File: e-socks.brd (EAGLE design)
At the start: 65.1 x 30 mm, 91 parts, among them IC1 CC2540, IC2 741G240DCK, IC3 TPS6300X, P2 TMAV433BAA, Q1 FA-20H(32MHz), Q2 ABS06, U2 MAX21000, X4 1296-T10

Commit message: erstes commit für diesen branch
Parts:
- removed C1: 100nF, rcl:C0402
- removed IC3: TPS6300X, m_vreg:S-PVSON-N10
- removed L1: CR32, inductors:CR32
- added LED3, LED4: Blue/2.9V@10mA, led:CHIP-LED0603
- added R8: 47RR, rcl:R0402
- C5, C6: value 10µF -> 22µF; device rcl:C0603 -> rcl:C0805
- R6: value 100R -> 47RR
- moved R6 24.7 mm to (19.6, 27.4), turned to 90 degrees
- moved L3 11.0 mm to (3.62, 16.6), turned to 270 degrees
- moved C9 10.5 mm to (6.29, 8.83)
- moved IC7 10.4 mm to (6.99, 10.7)
- moved R5 8.84 mm to (4.32, 8.64), turned to 90 degrees
- moved R3 6.46 mm to (3.68, 10.5), turned to 180 degrees
- moved C2 5.05 mm to (8.64, 14.4)
- moved C6 1.36 mm to (12.9, 10.8), turned to 270 degrees
- moved C5 0.77 mm to (11.0, 10.7), turned to 270 degrees
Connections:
- removed net N$10: C1.2, IC3.7, IC3.8, R6.2
- removed net VOUT: IC7.7
- net +5V: now also IC7.7; no longer IC3.1
- net 5V_ENABLE: now also IC7.2; no longer IC3.6
- net GND: now also LED3.C, LED4.C; no longer C1.1, IC3.3, IC3.9, IC3.PAD
- net HEATER1_PWR: now also R8.1
- net HEATER2_PWR: now also R6.1
- net N$1: now also LED3.A, R6.2; no longer IC3.4, L1.1
- net N$3: now also LED4.A, R8.2; no longer IC3.2, L1.2
- net N$4: now also IC7.3; no longer IC3.10
- net VBAT: no longer IC3.5, R6.1
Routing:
- net VBAT: track 56.3 -> 49.1 mm
- net +5V: track 1.65 -> 8.33 mm
- net N$4: track 7.31 -> 3.15 mm, vias 2 -> 0
- net N$1: track 3.42 -> 0.00 mm
- net N$3: track 3.42 -> 0.00 mm
- net N$10: track 3.20 -> 0.00 mm
- net N$6: track 0.00 -> 1.28 mm
- net 5V_ENABLE: track 31.9 -> 30.9 mm
- added copper zone on layer 1, net N$5

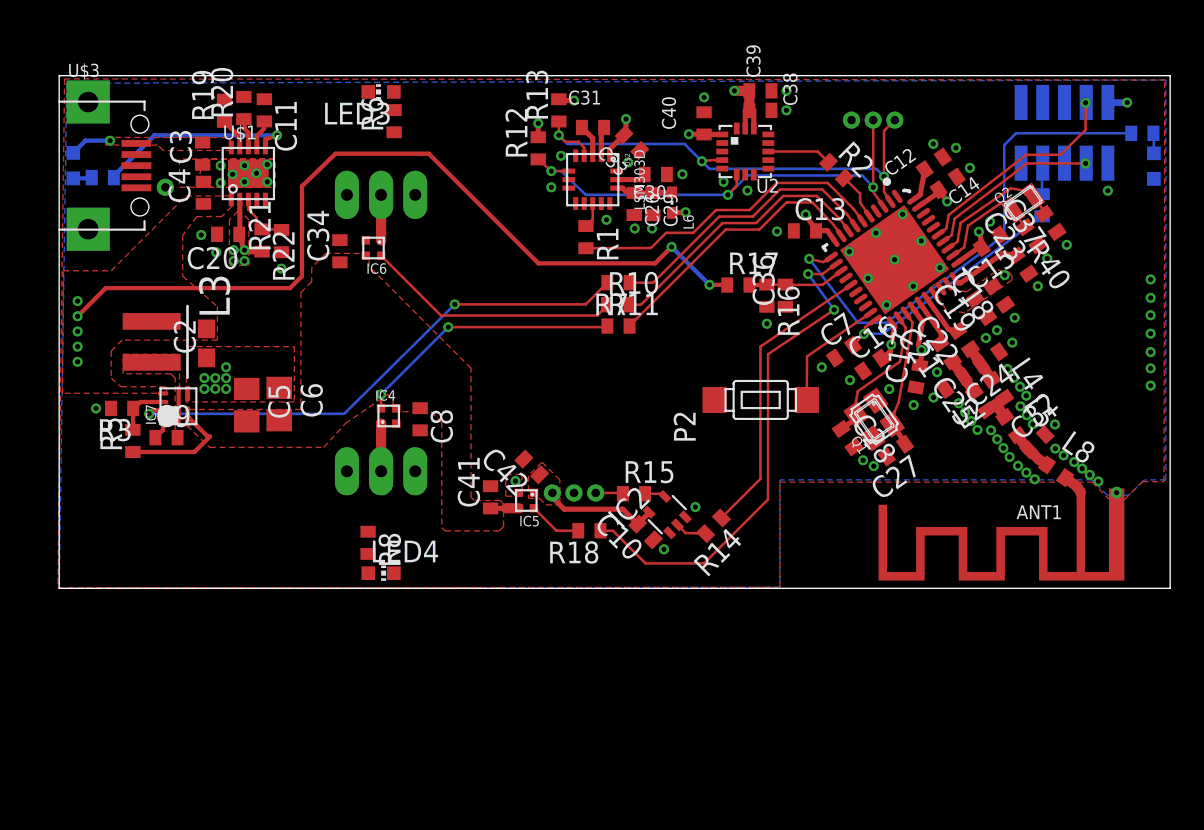
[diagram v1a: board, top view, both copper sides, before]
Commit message: taster getauscht, 2.5mm klinke hinzugefügt, noch nicht geroutet
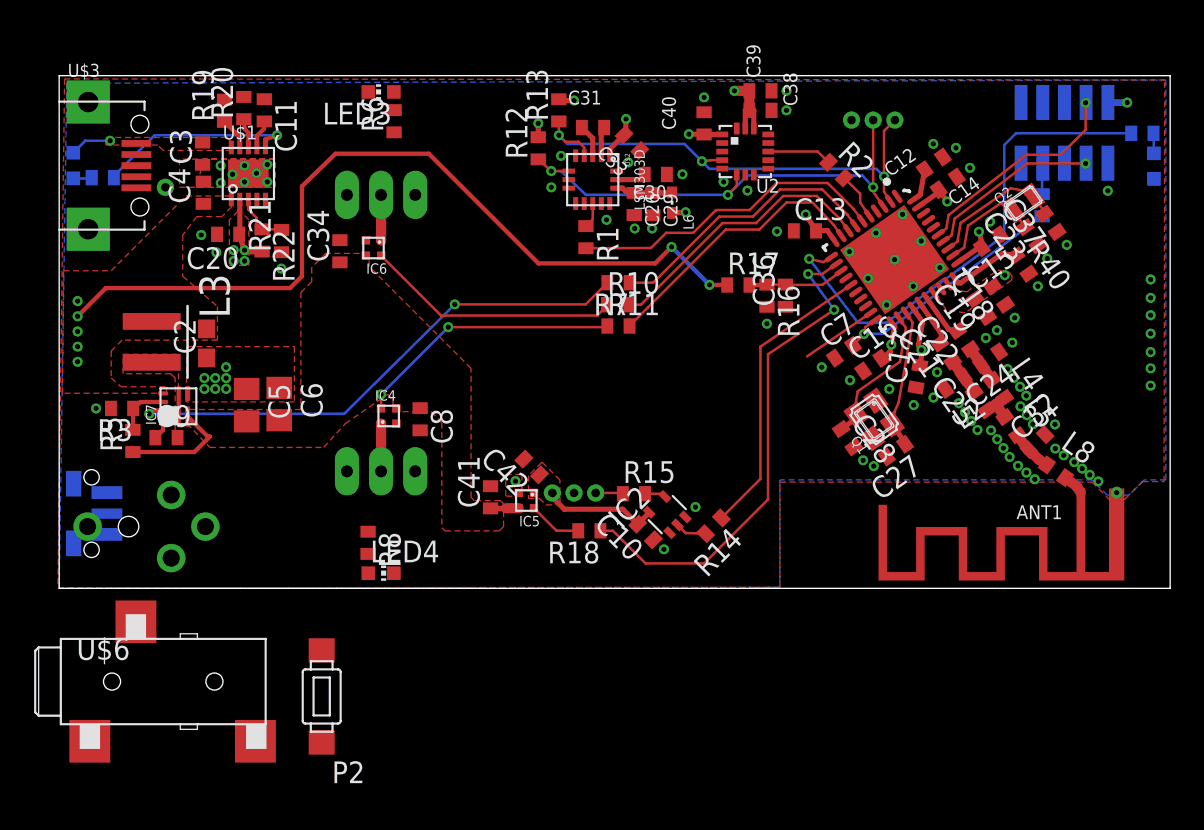
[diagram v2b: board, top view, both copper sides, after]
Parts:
- added S1: TL3340AF160QG, SamacSys_Parts:TL3340
- added U$6: SJ-2523-SMT, con-cuistack:SJ-2523-SMT
- added U$7: SJ-2503A, con-cuistack:SJ-2503
- moved P2 31.0 mm to (15.4, -6.33), turned to 180 degrees
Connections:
- net GND: now also S1.1, S1.3, U$6.1, U$7.1
- net LS2812_PWR: now also U$6.3, U$7.4
- net SW1: now also S1.2
- net WS2812B_OUT: now also U$6.2, U$7.2
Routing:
- net SW1: track 7.06 -> 4.50 mm
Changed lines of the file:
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@@
 <layer number="14" name="Route14" color="1" fill="6" visible="no" active="no"/>
 <layer number="15" name="Route15" color="4" fill="6" visible="no" active="yes"/>
-<layer number="16" name="Bottom" color="1" fill="1" visible="yes" active="yes"/>
+<layer number="16" name="Bottom" color="1" fill="1" visible="no" active="yes"/>
 <layer number="17" name="Pads" color="2" fill="1" visible="yes" active="yes"/>
 <layer number="18" name="Vias" color="2" fill="1" visible="yes" active="yes"/>
@@
 <layer number="22" name="bPlace" color="7" fill="1" visible="yes" active="yes"/>
 <layer number="23" name="tOrigins" color="15" fill="1" visible="yes" active="yes"/>
-<layer number="24" name="bOrigins" color="15" fill="1" visible="no" active="yes"/>
+<layer number="24" name="bOrigins" color="15" fill="1" visible="yes" active="yes"/>
 <layer number="25" name="tNames" color="7" fill="1" visible="no" active="yes"/>
 <layer number="26" name="bNames" color="7" fill="1" visible="no" active="yes"/>
@@
 <layer number="39" name="tKeepout" color="4" fill="11" visible="no" active="yes"/>
 <layer number="40" name="bKeepout" color="1" fill="11" visible="no" active="yes"/>
-<layer number="41" name="tRestrict" color="4" fill="10" visible="no" active="yes"/>
+<layer number="41" name="tRestrict" color="4" fill="10" visible="yes" active="yes"/>
 <layer number="42" name="bRestrict" color="1" fill="10" visible="no" active="yes"/>
 <layer number="43" name="vRestrict" color="2" fill="10" visible="no" active="yes"/>
@@
 <board>
 <plain>
+<wire x1="51.6255" y1="16.637" x2="52.705" y2="15.8115" width="0" layer="41"/>
 <wire x1="52.705" y1="15.8115" x2="56.007" y2="11.1125" width="0" layer="41"/>
 <wire x1="55.499" y1="10.7315" x2="56.896" y2="8.6995" width="0" layer="41"/>
@@
 <element name="Q1" library="crystal-epson" package="FA-20H" value="FA-20H(32MHz)" x="47.74906875" y="9.89306875" rot="R125"/>
 <element name="L8" library="rcl-2" package="L0402" value="3N0" x="58.402075" y="6.85911875" rot="R325"/>
-<element name="P2" library="switch-misc" package="TMAV433BAA" value="TMAV433BAA" x="41.100346875" y="11.036846875" rot="R90"/>
+<element name="P2" library="switch-misc" package="TMAV433BAA" value="TMAV433BAA" x="15.379153125" y="-6.334153125" rot="R180"/>
 <element name="C4" library="resistor" package="C0402" value="2,2µF" x="8.4455" y="23.1775" rot="R90"/>
 <element name="C3" library="rcl" package="C0402" value="4,7µF" x="8.404" y="25.465" rot="R90"/>
@@
 <element name="R8" library="rcl" package="R0402" value="47RR" x="18.0975" y="2.667" rot="R270"/>
 <element name="LED4" library="led" package="CHIP-LED0603" value="Blue/2.9V@10mA" x="18.8595" y="0.889" rot="R270"/>
+<element name="S1" library="SamacSys_Parts" package="TL3340" value="TL3340AF160QG" x="0.6985" y="4.3815" rot="MR90">
+<attribute name="DESCRIPTION" value="E-SWITCH - TL3340AF160QG. - SWITCH, TACTILE SPST 50mA, SMD GULL WING" x="0.6985" y="4.3815" size="1.778" layer="28" rot="MR90" display="off"/>
+<attribute name="HEIGHT" value="mm" x="0.6985" y="4.3815" size="1.778" layer="28" rot="MR90" display="off"/>
+<attribute name="MOUSER_PART_NUMBER" value="612-TL3340AF160QG" x="0.6985" y="4.3815" size="1.778" layer="28" rot="MR90" display="off"/>
+<attribute name="MANUFACTURER_NAME" value="E-Switch" x="0.6985" y="4.3815" size="1.778" layer="28" rot="MR90" display="off"/>
+<attribute name="MANUFACTURER_PART_NUMBER" value="TL3340AF160QG" x="0.6985" y="4.3815" size="1.778" layer="28" rot="MR90" display="off"/>
+</element>
+<element name="U$6" library="con-cuistack" package="SJ-2523-SMT" value="SJ-2523-SMT" x="6.096" y="-5.461" rot="R270"/>
+<element name="U$7" library="con-cuistack" package="SJ-2503" value="SJ-2503A" x="4.064" y="3.6195" rot="MR180"/>
 </elements>
 <signals>
@@
 <contactref element="L2" pad="2"/>
 <contactref element="P2" pad="P$1"/>
-<polygon width="0.254" layer="1" isolate="0.2" rank="2">
+<polygon width="0.254" layer="1" isolate="0.2" rank="3">
 <vertex x="0.3175" y="29.845"/>
 <vertex x="-0.07375" y="0.03175"/>
@@
 <contactref element="LED2" pad="C"/>
 <via x="28.829" y="23.495" extent="1-16" drill="0.3"/>
-<polygon width="0.3048" layer="16" isolate="0.254" rank="2">
+<polygon width="0.3048" layer="16" isolate="0.254" rank="3">
 <vertex x="42.2275" y="6.35"/>
 <vertex x="42.2275" y="0.0635"/>
@@
 <contactref element="LED3" pad="C"/>
 <contactref element="LED4" pad="C"/>
+<contactref element="S1" pad="3"/>
+<contactref element="S1" pad="1"/>
+<contactref element="U$6" pad="1"/>
+<contactref element="U$7" pad="1"/>
+<wire x1="37.7825" y1="28.7655" x2="15.379153125" y2="-9.032953125" width="0" layer="19" extent="1-1"/>
+<wire x1="1.796" y1="-8.961" x2="2.7985" y2="3.1565" width="0" layer="19" extent="1-16"/>
 </signal>
 <signal name="N$28">
@@
 <via x="53.886165625" y="20.889921875" extent="1-16" drill="0.3"/>
 <via x="52.0259125" y="22.6609625" extent="1-16" drill="0.3"/>
-<polygon width="0.254" layer="1" isolate="0.254" thermals="no" rank="2">
+<polygon width="0.254" layer="1" isolate="0.254" thermals="no">
 <vertex x="51.83158125" y="18.17801875"/>
 <vertex x="52.286859375" y="17.527815625"/>
@@
 <contactref element="IC1" pad="19"/>
 <wire x1="47.5315125" y1="16.1314875" x2="43.815" y2="13.589" width="0.15" layer="1"/>
-<wire x1="43.815" y1="13.589" x2="43.799146875" y2="11.036846875" width="0.15" layer="1"/>
+<contactref element="S1" pad="2"/>
+<wire x1="47.5315125" y1="16.1314875" x2="15.379153125" y2="-3.635353125" width="0" layer="19" extent="1-1"/>
+<wire x1="2.7985" y1="4.3815" x2="43.815" y2="13.589" width="0" layer="19" extent="1-16"/>
 </signal>
 <signal name="VBUS">
@@
 </polygon>
 <via x="2.9845" y="26.2255" extent="1-16" drill="0.3"/>
-<wire x1="1.524" y1="26.2255" x2="2.9845" y2="26.2255" width="0.254" layer="16"/>
+<wire x1="1.524" y1="26.2255" x2="2.9845" y2="26.2255" width="0.15" layer="16"/>
 <contactref element="U$3" pad="1"/>
-<wire x1="1.524" y1="26.2255" x2="1.524" y2="26.2135" width="0.254" layer="16"/>
-<wire x1="1.524" y1="26.2135" x2="0.8255" y2="25.515" width="0.254" layer="16"/>
+<wire x1="1.524" y1="26.2255" x2="1.524" y2="26.2135" width="0.15" layer="16"/>
+<wire x1="1.524" y1="26.2135" x2="0.8255" y2="25.515" width="0.15" layer="16"/>
 </signal>
 <signal name="VBAT">
@@
 <wire x1="12.08325" y1="26.30725" x2="12.7635" y2="26.543" width="0.254" layer="1"/>
 <wire x1="3.205" y1="24.06375" x2="3.205" y2="24.16" width="0.254" layer="16"/>
-<wire x1="3.205" y1="24.16" x2="5.588" y2="26.543" width="0.254" layer="16"/>
-<wire x1="5.588" y1="26.543" x2="12.7635" y2="26.543" width="0.254" layer="16"/>
+<wire x1="3.205" y1="24.16" x2="5.588" y2="26.543" width="0.15" layer="16"/>
+<wire x1="5.588" y1="26.543" x2="12.7635" y2="26.543" width="0.15" layer="16"/>
 <wire x1="12.7635" y1="26.543" x2="12.7635" y2="26.543" width="0" layer="19" extent="1-16"/>
 </signal>
@@
 <contactref element="R4" pad="1"/>
 <contactref element="LED1" pad="C"/>
-<wire x1="0.8255" y1="24.015" x2="1.85625" y2="24.015" width="0.254" layer="16"/>
+<wire x1="0.8255" y1="24.015" x2="1.85625" y2="24.015" width="0.15" layer="16"/>
 <wire x1="1.85625" y1="24.015" x2="1.905" y2="24.06375" width="0.254" layer="16"/>
 </signal>
@@
 <wire x1="33.023596875" y1="5.54309375" x2="32.978690625" y2="5.588" width="0.15" layer="1"/>
 <wire x1="32.978690625" y1="5.588" x2="31.4325" y2="5.588" width="0.15" layer="1"/>
+<contactref element="U$6" pad="2"/>
+<contactref element="U$7" pad="2"/>
+<wire x1="11.496" y1="-8.961" x2="31.4325" y2="5.588" width="0" layer="19" extent="1-1"/>
+<wire x1="6.564" y1="5.4695" x2="11.496" y2="-8.961" width="0" layer="19" extent="1-1"/>
 </signal>
 <signal name="N$50">
@@
 <wire x1="34.5628375" y1="4.45941875" x2="34.5628375" y2="4.430578125" width="0.3048" layer="1"/>
 <wire x1="34.5628375" y1="4.430578125" x2="33.893878125" y2="3.76161875" width="0.3048" layer="1"/>
+<contactref element="U$6" pad="3"/>
+<contactref element="U$7" pad="4"/>
+<wire x1="4.496" y1="-1.961" x2="8.564" y2="3.6195" width="0" layer="19" extent="1-1"/>
+<wire x1="27.8185" y1="5.5935" x2="8.564" y2="3.6195" width="0" layer="19" extent="1-1"/>
 </signal>
 <signal name="N$52">
@@
 <vertex x="14.1605" y="10.4775"/>
 <vertex x="7.493" y="10.4775"/>
-<vertex x="7.493" y="9.525"/>
+<vertex x="7.493" y="9.652"/>
 <vertex x="8.8265" y="8.255"/>
 <vertex x="15.494" y="8.255"/>
@@
 <polygon width="0.254" layer="1" thermals="no">
 <vertex x="3.7465" y="13.716"/>
-<vertex x="7.0485" y="13.716"/>
-<vertex x="7.0485" y="8.6995"/>
+<vertex x="6.985" y="13.716"/>
+<vertex x="6.985" y="8.6995"/>
 <vertex x="6.7945" y="8.6995"/>
 <vertex x="6.7945" y="12.319"/>

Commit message: routing fertig @home
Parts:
- removed P2: TMAV433BAA, switch-misc:TMAV433BAA
- removed U$6: SJ-2523-SMT, con-cuistack:SJ-2523-SMT
- added S2: TL3340AF160QG, SamacSys_Parts:TL3340
- moved S1 31.9 mm to (32.4, 0.57), turned to 0 degrees
- moved R15 24.7 mm to (9.16, 2.18)
- moved IC2 21.3 mm to (14.3, 3.03), turned to 180 degrees
- moved C10 18.4 mm to (15.9, 2.85), turned to 270 degrees
- moved C42 17.2 mm to (10.8, 4.03), turned to 0 degrees
- moved IC5 16.7 mm to (10.7, 6.29), turned to 0 degrees
- moved C41 12.2 mm to (13.1, 6.35), turned to 270 degrees
- moved R18 10.9 mm to (32.8, 14.1)
- moved R14 10.8 mm to (32.8, 12.9), turned to 180 degrees
- moved R45 3.78 mm to (62.4, 23.0)
- moved R6 3.39 mm to (22.9, 28.4)
- moved LED2 2.48 mm to (64.1, 22.3)
- moved C34 2.03 mm to (18.5, 19.7)
- moved C8 2.03 mm to (23.2, 9.91)
- moved IC4 2.03 mm to (21.3, 10.1)
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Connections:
- removed net N$33: R4.2, U$1.P6
- new net !CHRG: IC1.14, R4.2, U$1.P6
- new net SW2: IC1.18, S2.2
- net GND: now also S2.1, S2.3, U$1.P4, U$1.P5; no longer P2.P$1, U$6.1
- net LS2812_PWR: no longer U$6.3
- net SW1: no longer P2.P$2
- net WS2812B_OUT: now also U$7.3; no longer U$6.2, U$7.2
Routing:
- net !CHRG: track 0.00 -> 49.8 mm, vias 0 -> 2
- net SW2: track 0.00 -> 25.5 mm, vias 0 -> 1
- net LS2812_EN: track 3.13 -> 26.5 mm, vias 0 -> 2
- net SPI_MO: track 1.85 -> 23.8 mm, vias 0 -> 2
- net SW1: track 4.50 -> 24.2 mm, vias 0 -> 1
- net N$52: track 29.8 -> 14.8 mm, vias 2 -> 0
- net N$33: track 11.8 -> 0.00 mm
- net HEATER2_PWR: track 2.66 -> 9.34 mm, vias 0 -> 1
- net HEATER1_PWR: track 2.79 -> 9.40 mm, vias 0 -> 1
- net RED_LED: track 29.4 -> 32.3 mm
- net N$50: track 17.4 -> 14.6 mm
- net N$44: track 1.23 -> 3.86 mm
- net PWM2: track 15.0 -> 12.9 mm
- net PWM1: track 15.8 -> 13.8 mm
- net DD: track 12.8 -> 10.9 mm
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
